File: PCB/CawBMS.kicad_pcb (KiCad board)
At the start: 4 copper layers, 53.5 x 38 mm, 132 parts, among them CN1 SWD, CN2 I2C, CN3 SPI, CN4 USART, CN5 SWD, CN6 WAFER-SH1.0-6PWB, Q1 CSD13381F4, Q10 TP0610K-T1-GE3, Q2 CSD13381F4, Q3 CSD13381F4, Q4 CSD13381F4, Q5 CSD13381F4, Q6 BSC0702LS, Q7 BSC0702LS, Q8 BSC0702LS, Q9 BSC0702LS, SW1 B3U-1000P, SW2 B3U-1000P, SW3 B3U-1000P, U1 STM32F103CBTx, U2 TCAN1044DRBRQ1, U3 TPS61240DRVR, U4 BQ7692003PW, U5 CAN, X1 Crystal_16MHz_15pF_3P

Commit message: Signed-off-by: jasperThinkpad <2567434944@qq.com>
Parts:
- removed R40: 1M, Resistor_SMD:R_0402_1005Metric_Pad0.72x0.64mm_HandSolder
- removed REF**: OSHW-Logo2_9.8x8mm_SilkScreen, Symbol:OSHW-Logo2_9.8x8mm_SilkScreen
- removed U5: CAN, Rick_Connector:CONN-SMD_2P-P1.00_XUNPU_WAFER-SH1.0-2PWB
- added CN7: WAFER-SH1.0-6PWB, Rick_Connector:CONN-SMD_6P-P1.00_XUNPU_WAFER-SH1.0-6PWB, B.Cu at (88.0, 73.0)
- added R11: 0, Resistor_SMD:R_0402_1005Metric_Pad0.72x0.64mm_HandSolder, F.Cu at (101.0, 45.0)
- C10: value 0.22uF -> 4.7uF
- C11, C9: value 0.22uF -> 0.1uF; footprint Capacitor_SMD:C_0402_1005Metric_Pad0.74x0.62mm_HandSolder -> Capacitor_SMD:C_0603_1608Metric_Pad1.08x0.95mm_HandSolder
- C12: value 0.22uF -> 2.2uF
- C15: value 4.7uF -> 470pF
- C16: value 2.2uF -> 1uF
- C17: value 1uF -> 0.22uF
- C18: value 1uF -> 4.7uF
- C19: value 10uF -> 1uF; footprint Capacitor_SMD:C_0603_1608Metric_Pad1.08x0.95mm_HandSolder -> Capacitor_SMD:C_0402_1005Metric_Pad0.74x0.62mm_HandSolder
- C20: value 4.7uF -> 10uF; footprint Capacitor_SMD:C_0402_1005Metric_Pad0.74x0.62mm_HandSolder -> Capacitor_SMD:C_0603_1608Metric_Pad1.08x0.95mm_HandSolder
- C21, C22: value 0.1uF -> 0.22uF
- C24: value 470pF -> 0.1uF
- C25: footprint Capacitor_SMD:C_0603_1608Metric_Pad1.08x0.95mm_HandSolder -> Capacitor_SMD:C_0402_1005Metric_Pad0.74x0.62mm_HandSolder
- C26: value 0.1uF -> 0.22uF; footprint Capacitor_SMD:C_0603_1608Metric_Pad1.08x0.95mm_HandSolder -> Capacitor_SMD:C_0402_1005Metric_Pad0.74x0.62mm_HandSolder
- CN1: value SWD -> CAN; footprint Rick_Connector:CONN-SMD_4P-P1.00_WAFER-SH1.0-4PWB -> Rick_Connector:CONN-SMD_2P-P1.00_XUNPU_WAFER-SH1.0-2PWB
- CN2: value I2C -> SWD
- CN3: value SPI -> I2C; footprint Rick_Connector:CONN-SMD_6P-P1.00_XUNPU_WAFER-SH1.0-6PWB -> Rick_Connector:CONN-SMD_4P-P1.00_WAFER-SH1.0-4PWB
- CN4: value USART -> SPI; footprint Rick_Connector:CONN-SMD_4P-P1.00_WAFER-SH1.0-4PWB -> Rick_Connector:CONN-SMD_6P-P1.00_XUNPU_WAFER-SH1.0-6PWB
- CN5: value SWD -> USART
- CN6: value WAFER-SH1.0-6PWB -> POWER; footprint Rick_Connector:CONN-SMD_6P-P1.00_XUNPU_WAFER-SH1.0-6PWB -> Rick_Connector:CONN-SMD_4P-P1.00_WAFER-SH1.0-4PWB
- D10: value D_200V -> D_Zener_5.6V; footprint Diode_SMD:D_SMA_Handsoldering -> Diode_SMD:D_SOD-523
- D11: value D_100V -> D_Zener_16V; footprint Diode_SMD:D_SOD-323_HandSoldering -> Diode_SMD:D_SOD-523
- D12: value D_Zener_16V -> D_Zener_5.6V
- D4: value D_Zener_5.6V -> TVS_24V; footprint Diode_SMD:D_SOD-523 -> Diode_SMD:D_SMA_Handsoldering
- D5: value D_Zener_5.6V -> D_200V; footprint Diode_SMD:D_SOD-523 -> Diode_SMD:D_SMA_Handsoldering
- D9: value TVS_24V -> D_100V; footprint Diode_SMD:D_SMA_Handsoldering -> Diode_SMD:D_SOD-323_HandSoldering
- H6: value B- -> P+
- H7: value P+ -> B-
- Q10: value TP0610K-T1-GE3 -> BSC0702LS; footprint Package_TO_SOT_SMD:SOT-23 -> Rick_MOSFET:BSC0702LS_PG-TDSON-8_L5.0-W6.0-P1.27-BL-EP
- Q4: value CSD13381F4 -> TP0610K-T1-GE3; footprint Rick_MOSFET:CSD13381F4_PICOSTAR-3_L1.0-W0.6-P0.40-S0.65-BL-1 -> Package_TO_SOT_SMD:SOT-23
- Q6: value BSC0702LS -> CSD13381F4; footprint Rick_MOSFET:BSC0702LS_PG-TDSON-8_L5.0-W6.0-P1.27-BL-EP -> Rick_MOSFET:CSD13381F4_PICOSTAR-3_L1.0-W0.6-P0.40-S0.65-BL-1
- R1: value 10k -> 120
- R12, R15: value 28.7 -> 100
- R14: value 28.7 -> 10k
- R17: value 100 -> 499k
- R19, R27, R31: value 100 -> 10k
- R20: value 10k -> NTC 10k
- R22, R26: value 10k -> 28.7
- R28: value NTC 10k -> 1M
- R29: value 10k -> 100
- R3: value 0 -> 10k
- R30: value 100 -> 28.7
- R32: value 0.0015 -> 1M; footprint Resistor_SMD:R_2512_6332Metric_Pad1.40x3.35mm_HandSolder -> Resistor_SMD:R_0402_1005Metric_Pad0.72x0.64mm_HandSolder
- R33, R34: value 0.0015 -> 100; footprint Resistor_SMD:R_2512_6332Metric_Pad1.40x3.35mm_HandSolder -> Resistor_SMD:R_0402_1005Metric_Pad0.72x0.64mm_HandSolder
- R35: value 100 -> 1M
- R36, R39: value 1M -> 0.0015; footprint Resistor_SMD:R_0402_1005Metric_Pad0.72x0.64mm_HandSolder -> Resistor_SMD:R_2512_6332Metric_Pad1.40x3.35mm_HandSolder
- R37: value 0 -> 100
- R38: value 499k -> 0.0015; footprint Resistor_SMD:R_0402_1005Metric_Pad0.72x0.64mm_HandSolder -> Resistor_SMD:R_2512_6332Metric_Pad1.40x3.35mm_HandSolder
- R6: value 120 -> 10k
- R7: value 510 -> 0
- R8: value 10k -> 510
- U1: value STM32F103CBTx -> SIT1051AT/3; footprint Package_QFP:LQFP-48_7x7mm_P0.5mm -> Rick_CAN:ISO1044BDR_SOP-8
- U2: value TCAN1044DRBRQ1 -> STM32F103C_8-B_Tx; footprint Rick_CAN:TCAN1044DRBRQ1_DFN-8_L3.0-W3.0-P0.65-TL-EP2.4 -> Package_QFP:LQFP-48_7x7mm_P0.5mm
- moved C1 63.7 mm to (107.6, 47.0)
- moved C10 63.7 mm to (92.4, 46.8)
- moved C11 63.7 mm to (92.4, 49.8)
- moved C15 63.7 mm to (105.0, 56.7)
- moved C24 63.7 mm to (102.1, 49.4)
- moved C26 63.7 mm to (105.4, 66.5)
- moved C4 63.7 mm to (107.6, 45.8)
- moved C5 63.7 mm to (120.4, 49.0)
- moved C6 63.7 mm to (105.0, 54.2)
- moved C8 63.7 mm to (105.0, 51.7)
- moved CN5 63.7 mm to (125.8, 48.5)
- moved CN6 63.7 mm to (78.8, 49.8)
- moved L4 63.7 mm to (99.8, 66.5)
- moved L5 63.7 mm to (111.5, 66.5)
- moved Q3 63.7 mm to (86.1, 49.8)
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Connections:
- C1 pad 1: +3.3V -> +5V
- C10 pad 1: /BQ76920/VC4 -> +5V
- C10 pad 2: /BQ76920/VC3 -> GND
- C11 pad 1: /BQ76920/VC3 -> Net-(C11-Pad1)
- C11 pad 2: /BQ76920/VC2 -> PACK-
- C12 pad 1: /BQ76920/VC2 -> +3.3V
- C12 pad 2: /BQ76920/VC1 -> GND
- C13 pad 1: /BQ76920/VC1 -> /BQ76920/VC5
- C13 pad 2: /BQ76920/VC0 -> /BQ76920/VC4
- C14 pad 1: /BQ76920/VC0 -> /BQ76920/VC4
- C14 pad 2: GND -> /BQ76920/VC3
- C15 pad 1: +3.3V -> /ALERT
- C16 pad 1: +3.3V -> GND
- C16 pad 2: GND -> Net-(U4-CAP1)
- C17 pad 1: /BQ76920/BAT -> /BQ76920/VC3
- C17 pad 2: GND -> /BQ76920/VC2
- C18 pad 1: GND -> +3.3V
- C18 pad 2: Net-(U4-CAP1) -> GND
- C19 pad 1: Net-(U4-BAT) -> /BQ76920/BAT
- C20 pad 1: +5V -> Net-(U4-BAT)
- C21 pad 1: GND -> /BQ76920/VC2
- C21 pad 2: /BQ76920/SRP -> /BQ76920/VC1
- C22 pad 1: /BQ76920/SRP -> /BQ76920/VC1
- C22 pad 2: /BQ76920/SRN -> /BQ76920/VC0
- C23 pad 1: /BQ76920/SRN -> GND
- C23 pad 2: GND -> /BQ76920/SRP
- C24 pad 1: /ALERT -> /BQ76920/SRP
- C24 pad 2: GND -> /BQ76920/SRN
- C25 pad 1: Net-(C25-Pad1) -> /BQ76920/SRN
- C25 pad 2: Net-(C25-Pad2) -> GND
- C26 pad 1: Net-(C25-Pad2) -> /BQ76920/VC0
- C26 pad 2: PACK- -> GND
- C27 pad 1: PACK+ -> Net-(C27-Pad1)
- C3 pad 1: +3.3V -> /RESET
- C5 pad 1: +5V -> +3.3V
- C6 pad 1: +3.3VA -> +3.3V
- C8 pad 1: /RESET -> +3.3VA
- C9 pad 1: /BQ76920/VC5 -> PACK+
- C9 pad 2: /BQ76920/VC4 -> Net-(C11-Pad1)
- CN1 pad 1: GND -> /CAN_N
- CN1 pad 2: GND -> /CAN_P
- CN1 pad 3: +3.3V -> unconnected-(CN1-Pad3)
- CN1 pad 4: +5V -> unconnected-(CN1-Pad4)
- CN2 pad 1: /I2C2_SDA -> /SWDIO
- CN2 pad 2: /I2C2_SCL -> /SWCLK
- CN3 pad 1: /SPI1_NSS -> /I2C2_SDA
- CN3 pad 2: /SPI1_SCK -> /I2C2_SCL
- CN3 pad 3: /SPI1_MISO -> GND
- CN3 pad 4: /SPI1_MOSI -> +3.3V
- CN3 pad 5: GND -> unconnected-(CN3-Pad5)
- CN3 pad 6: +3.3V -> unconnected-(CN3-Pad6)
- CN4 pad 1: /USART1_TX -> /SPI1_NSS
- CN4 pad 2: /USART1_RX -> /SPI1_SCK
- CN4 pad 3: GND -> /SPI1_MISO
- CN4 pad 4: +3.3V -> /SPI1_MOSI
- CN4 pad 5: unconnected-(CN4-Pad5) -> GND
- CN4 pad 6: unconnected-(CN4-Pad6) -> +3.3V
- CN5 pad 1: /SWDIO -> /USART1_TX
- CN5 pad 2: /SWCLK -> /USART1_RX
- CN6 pad 1: /BQ76920/BAT -> GND
- CN6 pad 2: Net-(D4-A) -> GND
- CN6 pad 3: Net-(D5-A) -> +3.3V
- CN6 pad 4: Net-(D6-A) -> +5V
- CN6 pad 5: Net-(D7-A) -> unconnected-(CN6-Pad5)
- CN6 pad 6: Net-(D8-A) -> unconnected-(CN6-Pad6)
- D10 pad 1: PACK+ -> Net-(D10-K)
- D10 pad 2: PACK- -> Net-(D10-A)
- D11 pad 2: Net-(D11-A) -> PACK-
- D12 pad 1: Net-(D11-K) -> Net-(D12-K)
- D12 pad 2: PACK- -> Net-(D12-A)
- D4 pad 1: Net-(D4-K) -> -BATT
- D4 pad 2: Net-(D4-A) -> PACK+
- D5 pad 1: Net-(D5-K) -> PACK+
- D5 pad 2: Net-(D5-A) -> PACK-
- D9 pad 1: -BATT -> Net-(D11-K)
- D9 pad 2: PACK+ -> Net-(D9-A)
- H6 pad 1: -BATT -> PACK+
- H7 pad 1: PACK+ -> -BATT
- L3 pad 2: Net-(Q7-G) -> Net-(Q9-G)
- L4 pad 2: Net-(Q6-G) -> Net-(Q7-G)
- L6 pad 2: Net-(Q9-G) -> Net-(Q10-G)
- Q1 pad 1: Net-(D4-K) -> Net-(D6-K)
- Q1 pad 2: Net-(D4-A) -> Net-(D6-A)
- Q10 pad 1: GND -> PACK-
- Q10 pad 2: /BQ76920/CHG -> PACK-
- Q10 pad 3: Net-(D11-A) -> PACK-
- Q2 pad 1: Net-(D5-K) -> Net-(D7-K)
- Q2 pad 2: Net-(D5-A) -> Net-(D7-A)
- Q3 pad 1: Net-(D6-K) -> Net-(D8-K)
- Q3 pad 2: Net-(D6-A) -> Net-(D8-A)
- Q4 pad 1: Net-(D7-K) -> GND
- Q4 pad 2: Net-(D7-A) -> /BQ76920/CHG
- Q4 pad 3: Net-(Q4-D) -> Net-(D9-A)
- Q5 pad 1: Net-(D8-K) -> Net-(D10-K)
- Q5 pad 2: Net-(D8-A) -> Net-(D10-A)
- Q6 pad 1: Net-(C25-Pad1) -> Net-(D12-K)
- Q6 pad 2: Net-(C25-Pad1) -> Net-(D12-A)
- Q6 pad 3: Net-(C25-Pad1) -> Net-(Q6-D)
- Q7 pad 1: Net-(C25-Pad1) -> Net-(C27-Pad1)
- Q7 pad 2: Net-(C25-Pad1) -> Net-(C27-Pad1)
- Q7 pad 3: Net-(C25-Pad1) -> Net-(C27-Pad1)
- Q7 pad 5: Net-(Q6-D-Pad5) -> Net-(Q10-D-Pad5)
- Q7 pad 6: Net-(Q6-D-Pad5) -> Net-(Q10-D-Pad5)
- Q7 pad 7: Net-(Q6-D-Pad5) -> Net-(Q10-D-Pad5)
- Q7 pad 8: Net-(Q6-D-Pad5) -> Net-(Q10-D-Pad5)
- Q8 pad 5: Net-(Q6-D-Pad5) -> Net-(Q10-D-Pad5)
- Q8 pad 6: Net-(Q6-D-Pad5) -> Net-(Q10-D-Pad5)
- Q8 pad 7: Net-(Q6-D-Pad5) -> Net-(Q10-D-Pad5)
- Q8 pad 8: Net-(Q6-D-Pad5) -> Net-(Q10-D-Pad5)
- Q9 pad 1: PACK- -> Net-(C27-Pad1)
- Q9 pad 2: PACK- -> Net-(C27-Pad1)
- Q9 pad 3: PACK- -> Net-(C27-Pad1)
- Q9 pad 5: Net-(Q6-D-Pad5) -> Net-(Q10-D-Pad5)
- Q9 pad 6: Net-(Q6-D-Pad5) -> Net-(Q10-D-Pad5)
- Q9 pad 7: Net-(Q6-D-Pad5) -> Net-(Q10-D-Pad5)
- Q9 pad 8: Net-(Q6-D-Pad5) -> Net-(Q10-D-Pad5)
- R1 pad 1: GND -> /CAN_N
- R1 pad 2: Net-(U1-PB2) -> /CAN_P
- R12 pad 2: Net-(Q1-D) -> /BQ76920/VC5
- R13 pad 1: Net-(D4-A) -> /BQ76920/BAT
- R13 pad 2: Net-(Q2-D) -> Net-(Q1-D)
- R14 pad 1: Net-(D5-A) -> Net-(D6-K)
- R14 pad 2: Net-(Q3-D) -> /BQ76920/VC4
- R15 pad 2: Net-(Q4-D) -> /BQ76920/VC4
- R16 pad 1: Net-(D7-A) -> Net-(D6-A)
- R16 pad 2: Net-(Q5-D) -> Net-(Q2-D)
- R17 pad 1: /BQ76920/BAT -> GND
- R17 pad 2: /BQ76920/VC5 -> /ALERT
- R18 pad 1: Net-(D4-K) -> Net-(D7-K)
- R18 pad 2: /BQ76920/VC4 -> /BQ76920/VC3
- R19 pad 1: Net-(D4-A) -> Net-(R19-Pad1)
- R19 pad 2: /BQ76920/VC4 -> Net-(U4-TS1)
- R2 pad 2: Net-(U1-BOOT0) -> Net-(U2-BOOT0)
- R20 pad 1: Net-(D5-K) -> GND
- R20 pad 2: /BQ76920/VC3 -> Net-(U4-TS1)
- R21 pad 1: Net-(D5-A) -> Net-(D7-A)
- R22 pad 1: Net-(D6-K) -> Net-(D7-A)
- R22 pad 2: /BQ76920/VC2 -> Net-(Q3-D)
- R23 pad 1: Net-(D6-A) -> /BQ76920/BAT
- R23 pad 2: /BQ76920/VC2 -> Net-(U4-BAT)
- R24 pad 1: Net-(D7-K) -> Net-(D8-K)
- R24 pad 2: /BQ76920/VC1 -> /BQ76920/VC2
- R25 pad 1: Net-(D7-A) -> Net-(D8-A)
- R25 pad 2: /BQ76920/VC1 -> /BQ76920/VC2
- R26 pad 1: Net-(D8-K) -> Net-(D8-A)
- R26 pad 2: /BQ76920/VC0 -> Net-(Q5-D)
- R27 pad 1: Net-(D8-A) -> Net-(D10-K)
- R27 pad 2: /BQ76920/VC0 -> /BQ76920/VC1
- R28 pad 1: GND -> Net-(D11-K)
- R28 pad 2: Net-(U4-TS1) -> Net-(D9-A)
- R29 pad 1: Net-(R29-Pad1) -> Net-(D10-A)
- R29 pad 2: Net-(U4-TS1) -> /BQ76920/VC1
- R3 pad 1: Net-(U1-VSSA) -> +3.3V
- R3 pad 2: GND -> /I2C1_SCL
- R30 pad 1: /BQ76920/BAT -> Net-(D10-A)
- R30 pad 2: Net-(U4-BAT) -> Net-(Q6-D)
- R31 pad 1: -BATT -> Net-(D12-K)
- R31 pad 2: /BQ76920/SRP -> /BQ76920/VC0
- R32 pad 1: -BATT -> PACK-
- R32 pad 2: Net-(C25-Pad1) -> Net-(D11-K)
- R33 pad 2: Net-(C25-Pad1) -> /BQ76920/SRP
- R34 pad 1: -BATT -> Net-(C27-Pad1)
- R34 pad 2: Net-(C25-Pad1) -> /BQ76920/SRN
- R35 pad 1: Net-(C25-Pad1) -> Net-(C27-Pad1)
- R35 pad 2: /BQ76920/SRN -> /BQ76920/DSG
- R36 pad 1: Net-(C25-Pad1) -> -BATT
- R36 pad 2: /BQ76920/DSG -> Net-(C27-Pad1)
- R37 pad 1: -BATT -> Net-(D12-A)
- R37 pad 2: GND -> /BQ76920/VC0
- R38 pad 1: GND -> -BATT
- R38 pad 2: /ALERT -> Net-(C27-Pad1)
- R39 pad 1: Net-(D11-K) -> -BATT
- R39 pad 2: Net-(D11-A) -> Net-(C27-Pad1)
- R4 pad 2: /I2C1_SCL -> /I2C1_SDA
- R5 pad 1: +3.3V -> GND
- R5 pad 2: /I2C1_SDA -> Net-(U2-PB2)
- R6 pad 1: /CAN_N -> +3.3V
- R6 pad 2: /CAN_P -> /RESET
- R7 pad 1: Net-(D1-K) -> Net-(U2-VSSA)
- R7 pad 2: /LED_A -> GND
- R8 pad 1: +3.3V -> Net-(D1-K)
- R8 pad 2: /RESET -> /LED_A
- SW3 pad 2: Net-(R29-Pad1) -> Net-(R19-Pad1)
- U1 pad 1: +3.3V -> /CAN_TX
- U1 pad 2: /ALERT -> GND
- U1 pad 3: /LED_A -> +5V
- U1 pad 4: /LED_B -> /CAN_RX
- U1 pad 5: /HSE_IN -> +3.3V
- U1 pad 6: /HSE_OUT -> /CAN_N
- U1 pad 7: /RESET -> /CAN_P
- U1 pad 8: Net-(U1-VSSA) -> /CAN_S
- U2 pad 1: /CAN_TX -> +3.3V
- U2 pad 2: GND -> /ALERT
- U2 pad 3: +5V -> /LED_A
- U2 pad 4: /CAN_RX -> /LED_B
- U2 pad 5: +3.3V -> /HSE_IN
- U2 pad 6: /CAN_N -> /HSE_OUT
- U2 pad 7: /CAN_P -> /RESET
- U2 pad 8: /CAN_STB -> Net-(U2-VSSA)
- U2 pad 9: GND -> +3.3VA
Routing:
- net +5V: track 51.5 -> 0.00 mm, vias 3 -> 0
- net GND: track 48.4 -> 0.00 mm, vias 45 -> 0
- net /BQ76920/BAT: track 43.9 -> 0.00 mm, vias 2 -> 0
- net +3.3V: track 42.2 -> 0.00 mm, vias 22 -> 0
- net /BQ76920/VC1: track 37.2 -> 0.00 mm, vias 2 -> 0
- net /KEY_A: track 34.3 -> 0.00 mm, vias 2 -> 0
- net /RESET: track 28.7 -> 0.00 mm
- net Net-(R29-Pad1): track 26.1 -> 0.00 mm
- net /ALERT: track 25.9 -> 0.00 mm, vias 2 -> 0
- net /I2C1_SDA: track 20.0 -> 0.00 mm, vias 2 -> 0
- net /BQ76920/VC4: track 19.2 -> 0.00 mm
- net /I2C1_SCL: track 18.5 -> 0.00 mm, vias 2 -> 0
- net /BQ76920/VC5: track 18.0 -> 0.00 mm
- net Net-(D8-A): track 17.8 -> 0.00 mm
- net /I2C2_SCL: track 16.9 -> 0.00 mm, vias 2 -> 0
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- removed copper zone on In2.Cu, net +3.3V
- removed copper zone on B.Cu, net -BATT
- removed copper zone on F.Cu, net -BATT
- removed copper zone on In1.Cu, net -BATT
- removed copper zone on In2.Cu, net -BATT
- removed copper zone on In1.Cu, net GND
- removed copper zone on B.Cu, net Net-(C25-Pad1)
- removed copper zone on F.Cu, net Net-(C25-Pad1)
- removed copper zone on In1.Cu, net Net-(C25-Pad1)
- removed copper zone on In2.Cu, net Net-(C25-Pad1)
- removed copper zone on F.Cu, net Net-(Q6-D-Pad5)
- removed copper zone on In1.Cu, net Net-(Q6-D-Pad5)
- removed copper zone on B.Cu, net PACK+
- removed copper zone on F.Cu, net PACK+
- removed copper zone on In1.Cu, net PACK+
- removed copper zone on In2.Cu, net PACK+
- removed copper zone on B.Cu, net PACK-
- removed copper zone on F.Cu, net PACK-
- removed copper zone on In1.Cu, net PACK-
- removed copper zone on In2.Cu, net PACK-

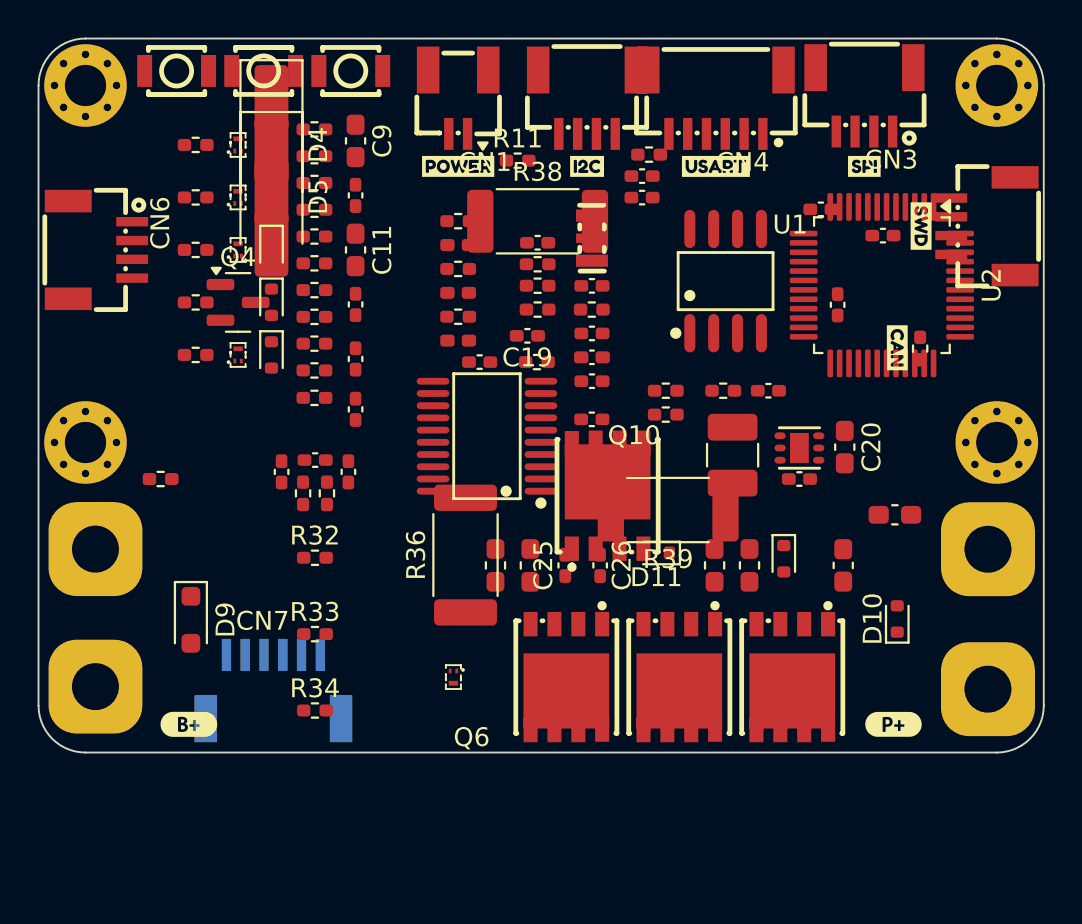
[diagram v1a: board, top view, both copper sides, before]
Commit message: 3.5 布局完成
Signed-off-by: jasper <2567434944@qq.com>
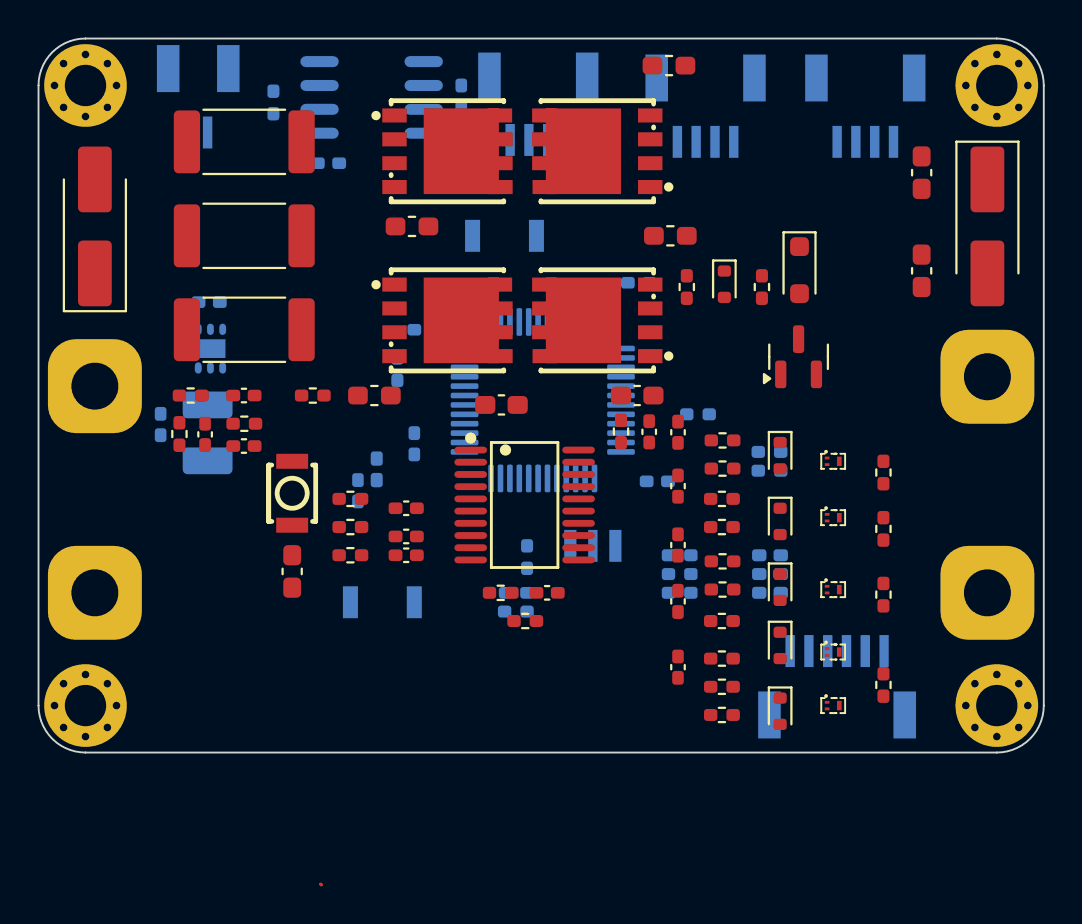
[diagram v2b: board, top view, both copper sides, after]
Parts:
- removed CN6: POWER, Rick_Connector:CONN-SMD_4P-P1.00_WAFER-SH1.0-4PWB
- removed CN7: WAFER-SH1.0-6PWB, Rick_Connector:CONN-SMD_6P-P1.00_XUNPU_WAFER-SH1.0-6PWB
- removed G***: LOGO, Rick_Logo:guaik_logo_black_8x8
- removed kibuzzard-6577EBC9: G***, kibuzzard-6577EBC9
- removed kibuzzard-6577F12B: G***, kibuzzard-6577F12B
- removed kibuzzard-6577F182: G***, kibuzzard-6577F182
- removed kibuzzard-6577F8B5: G***, kibuzzard-6577F8B5
- removed kibuzzard-6582907D: G***, kibuzzard-6582907D
- removed kibuzzard-65829086: G***, kibuzzard-65829086
- removed kibuzzard-65902364: G***, kibuzzard-65902364
- added kibuzzard-67C7CF73: G***, kibuzzard-67C7CF73, B.Cu at (97.0, 73.5)
- C1, C2, C3, C6, C7, C8, CN2, D1, D2, D3, R1, R10, R2, R3, R4, R5, R6, R7, R8, R9, U1, U2, U3, X1, kibuzzard-6577EBAB, kibuzzard-6577EC0F, kibuzzard-6577EC47, kibuzzard-658FE662, kibuzzard-658FE679: moved to B.Cu
- C10: value 4.7uF -> 0.1uF; moved to B.Cu
- C12: value 2.2uF -> 0.1uF; footprint Capacitor_SMD:C_0402_1005Metric_Pad0.74x0.62mm_HandSolder -> Capacitor_SMD:C_0603_1608Metric_Pad1.08x0.95mm_HandSolder
- C13: value 0.22uF -> 470pF
- C14, C17: value 0.22uF -> 1uF
- C15: value 470pF -> 0.22uF
- C16: value 1uF -> 4.7uF
- C18: value 4.7uF -> 10uF; footprint Capacitor_SMD:C_0402_1005Metric_Pad0.74x0.62mm_HandSolder -> Capacitor_SMD:C_0603_1608Metric_Pad1.08x0.95mm_HandSolder
- C19: value 1uF -> 0.22uF
- C20: value 10uF -> 0.22uF; footprint Capacitor_SMD:C_0603_1608Metric_Pad1.08x0.95mm_HandSolder -> Capacitor_SMD:C_0402_1005Metric_Pad0.74x0.62mm_HandSolder
- C22: value 0.22uF -> 0.1uF
- C25: value 0.1uF -> 0.22uF
- C4: value 0.1uF -> 4.7uF; moved to B.Cu
- C5: value 0.1uF -> 2.2uF; moved to B.Cu
- C9: footprint Capacitor_SMD:C_0603_1608Metric_Pad1.08x0.95mm_HandSolder -> Capacitor_SMD:C_0402_1005Metric_Pad0.74x0.62mm_HandSolder; moved to B.Cu
- CN1: value CAN -> USART; footprint Rick_Connector:CONN-SMD_2P-P1.00_XUNPU_WAFER-SH1.0-2PWB -> Rick_Connector:CONN-SMD_4P-P1.00_WAFER-SH1.0-4PWB; moved to B.Cu
- CN3: value I2C -> CAN; footprint Rick_Connector:CONN-SMD_4P-P1.00_WAFER-SH1.0-4PWB -> Rick_Connector:CONN-SMD_2P-P1.00_XUNPU_WAFER-SH1.0-2PWB; moved to B.Cu
- CN4: value SPI -> POWER; footprint Rick_Connector:CONN-SMD_6P-P1.00_XUNPU_WAFER-SH1.0-6PWB -> Rick_Connector:CONN-SMD_4P-P1.00_WAFER-SH1.0-4PWB; moved to B.Cu
- CN5: value USART -> WAFER-SH1.0-6PWB; footprint Rick_Connector:CONN-SMD_4P-P1.00_WAFER-SH1.0-4PWB -> Rick_Connector:CONN-SMD_6P-P1.00_XUNPU_WAFER-SH1.0-6PWB; moved to B.Cu
- D10: value D_Zener_5.6V -> D_Zener_16V
- D11: value D_Zener_16V -> D_Zener_5.6V
- D8: value D_Zener_5.6V -> D_100V; footprint Diode_SMD:D_SOD-523 -> Diode_SMD:D_SOD-323_HandSoldering
- D9: value D_100V -> D_Zener_5.6V; footprint Diode_SMD:D_SOD-323_HandSoldering -> Diode_SMD:D_SOD-523
- H6: value P+ -> B-
- H7: value B- -> P+
- L1: value 39nH -> 1uH; footprint Inductor_SMD:L_0402_1005Metric_Pad0.77x0.64mm_HandSolder -> Inductor_SMD:L_1210_3225Metric_Pad1.42x2.65mm_HandSolder; moved to B.Cu
- L2: value 1uH -> 39nH; footprint Inductor_SMD:L_1210_3225Metric_Pad1.42x2.65mm_HandSolder -> Inductor_SMD:L_0402_1005Metric_Pad0.77x0.64mm_HandSolder; moved to B.Cu
- Q3: value CSD13381F4 -> TP0610K-T1-GE3; footprint Rick_MOSFET:CSD13381F4_PICOSTAR-3_L1.0-W0.6-P0.40-S0.65-BL-1 -> Package_TO_SOT_SMD:SOT-23
- Q4: value TP0610K-T1-GE3 -> CSD13381F4; footprint Package_TO_SOT_SMD:SOT-23 -> Rick_MOSFET:CSD13381F4_PICOSTAR-3_L1.0-W0.6-P0.40-S0.65-BL-1
- Q6: value CSD13381F4 -> BSC0702LS; footprint Rick_MOSFET:CSD13381F4_PICOSTAR-3_L1.0-W0.6-P0.40-S0.65-BL-1 -> Rick_MOSFET:BSC0702LS_PG-TDSON-8_L5.0-W6.0-P1.27-BL-EP
- Q8: value BSC0702LS -> CSD13381F4; footprint Rick_MOSFET:BSC0702LS_PG-TDSON-8_L5.0-W6.0-P1.27-BL-EP -> Rick_MOSFET:CSD13381F4_PICOSTAR-3_L1.0-W0.6-P0.40-S0.65-BL-1
- R12: value 100 -> 499k
- R13: value 28.7 -> 10k
- R14: value 10k -> NTC 10k
- R17: value 499k -> 100
- R19, R31: value 10k -> 100
- R20: value NTC 10k -> 28.7
- R21: value 100 -> 10k
- R22, R26, R30: value 28.7 -> 100
- R23: value 100 -> 28.7
- R25, R29: value 100 -> 1M
- R27: value 10k -> 28.7
- R28: value 1M -> 10k
- R34, R37: value 100 -> 0.0015; footprint Resistor_SMD:R_0402_1005Metric_Pad0.72x0.64mm_HandSolder -> Resistor_SMD:R_2512_6332Metric_Pad1.40x3.35mm_HandSolder
- R35: value 1M -> 28.7
- R38: value 0.0015 -> 10k; footprint Resistor_SMD:R_2512_6332Metric_Pad1.40x3.35mm_HandSolder -> Resistor_SMD:R_0402_1005Metric_Pad0.72x0.64mm_HandSolder
- R39: value 0.0015 -> 100; footprint Resistor_SMD:R_2512_6332Metric_Pad1.40x3.35mm_HandSolder -> Resistor_SMD:R_0402_1005Metric_Pad0.72x0.64mm_HandSolder
- SW1, SW2: value B3U-1000P -> pro:7de6de4c8dc5470396d8d3e1a8ec5922; moved to B.Cu
- SW3: value B3U-1000P -> pro:7de6de4c8dc5470396d8d3e1a8ec5922
- moved Q1 43.5 mm to (117.8, 74.0), turned to -90 degrees
- moved Q2 39.9 mm to (117.8, 71.2), turned to -90 degrees
- moved C5 39.7 mm to (82.0, 59.0), turned to 90 degrees
- moved R20 39.5 mm to (120.5, 72.9), turned to 90 degrees
- moved kibuzzard-6577EC47 38.4 mm to (84.0, 45.6), turned to 180 degrees
- moved D5 38.1 mm to (126.0, 48.5)
- moved D6 36.6 mm to (115.0, 74.3)
- moved R19 35.7 mm to (111.9, 74.5), turned to 180 degrees
- moved R18 35.6 mm to (111.9, 73.0), turned to 180 degrees
- moved CN3 35.5 mm to (84.0, 41.8), turned to 0 degrees
- moved Q4 35.2 mm to (117.8, 67.8), turned to -90 degrees
- moved R23 34.3 mm to (120.5, 68.1), turned to 90 degrees
- moved Q5 32.8 mm to (117.8, 64.0), turned to -90 degrees
- moved D7 32.7 mm to (115.0, 70.8)
- moved U3 31.8 mm to (84.7, 55.0), turned to -90 degrees
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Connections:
- C10 pad 1: +5V -> +3.3VA
- C11 pad 1: Net-(C11-Pad1) -> PACK+
- C11 pad 2: PACK- -> Net-(C11-Pad2)
- C12 pad 1: +3.3V -> Net-(C11-Pad2)
- C12 pad 2: GND -> PACK-
- C13 pad 1: /BQ76920/VC5 -> /ALERT
- C13 pad 2: /BQ76920/VC4 -> GND
- C14 pad 1: /BQ76920/VC4 -> GND
- C14 pad 2: /BQ76920/VC3 -> Net-(U4-CAP1)
- C15 pad 1: /ALERT -> /BQ76920/VC5
- C15 pad 2: GND -> /BQ76920/VC4
- C16 pad 1: GND -> +3.3V
- C16 pad 2: Net-(U4-CAP1) -> GND
- C17 pad 1: /BQ76920/VC3 -> /BQ76920/BAT
- C17 pad 2: /BQ76920/VC2 -> GND
- C18 pad 1: +3.3V -> Net-(U4-BAT)
- C19 pad 1: /BQ76920/BAT -> /BQ76920/VC4
- C19 pad 2: GND -> /BQ76920/VC3
- C20 pad 1: Net-(U4-BAT) -> /BQ76920/VC3
- C20 pad 2: GND -> /BQ76920/VC2
- C22 pad 1: /BQ76920/VC1 -> GND
- C22 pad 2: /BQ76920/VC0 -> /BQ76920/SRP
- C23 pad 1: GND -> /BQ76920/SRP
- C23 pad 2: /BQ76920/SRP -> /BQ76920/SRN
- C24 pad 1: /BQ76920/SRP -> /BQ76920/SRN
- C24 pad 2: /BQ76920/SRN -> GND
- C25 pad 1: /BQ76920/SRN -> /BQ76920/VC1
- C25 pad 2: GND -> /BQ76920/VC0
- C4 pad 1: +3.3V -> +5V
- C8 pad 1: +3.3VA -> +3.3V
- C9 pad 1: PACK+ -> +3.3V
- C9 pad 2: Net-(C11-Pad1) -> GND
- CN1 pad 1: /CAN_N -> /USART1_TX
- CN1 pad 2: /CAN_P -> /USART1_RX
- CN1 pad 3: unconnected-(CN1-Pad3) -> GND
- CN1 pad 4: unconnected-(CN1-Pad4) -> +3.3V
- CN3 pad 1: /I2C2_SDA -> /CAN_N
- CN3 pad 2: /I2C2_SCL -> /CAN_P
- CN3 pad 3: GND -> unconnected-(CN3-Pad3)
- CN3 pad 4: +3.3V -> unconnected-(CN3-Pad4)
- CN4 pad 1: /SPI1_NSS -> GND
- CN4 pad 2: /SPI1_SCK -> GND
- CN4 pad 3: /SPI1_MISO -> +3.3V
- CN4 pad 4: /SPI1_MOSI -> +5V
- CN4 pad 5: GND -> unconnected-(CN4-Pad5)
- CN4 pad 6: +3.3V -> unconnected-(CN4-Pad6)
- CN5 pad 1: /USART1_TX -> /BQ76920/BAT
- CN5 pad 2: /USART1_RX -> Net-(D6-A)
- CN5 pad 3: GND -> Net-(D7-A)
- CN5 pad 4: +3.3V -> Net-(D9-A)
- CN5 pad 5: unconnected-(CN5-Pad5) -> Net-(D11-A)
- CN5 pad 6: unconnected-(CN5-Pad6) -> Net-(D12-A)
- D10 pad 2: Net-(D10-A) -> PACK-
- D11 pad 2: PACK- -> Net-(D11-A)
- D8 pad 1: Net-(D8-K) -> Net-(D10-K)
- D9 pad 1: Net-(D11-K) -> Net-(D9-K)
- H6 pad 1: PACK+ -> -BATT
- H7 pad 1: -BATT -> PACK+
- L1 pad 2: +3.3VA -> Net-(U3-L)
- L2 pad 2: Net-(U3-L) -> +3.3VA
- L4 pad 2: Net-(Q7-G) -> Net-(Q6-G)
- L5 pad 1: Net-(D11-K) -> Net-(D10-K)
- L5 pad 2: Net-(Q8-G) -> Net-(Q7-G)
- L6 pad 1: Net-(D11-K) -> Net-(D10-K)
- Q3 pad 1: Net-(D8-K) -> GND
- Q3 pad 2: Net-(D8-A) -> /BQ76920/CHG
- Q3 pad 3: Net-(Q3-D) -> Net-(D8-A)
- Q4 pad 1: GND -> Net-(D9-K)
- Q4 pad 2: /BQ76920/CHG -> Net-(D9-A)
- Q4 pad 3: Net-(D9-A) -> Net-(Q4-D)
- Q5 pad 1: Net-(D10-K) -> Net-(D11-K)
- Q5 pad 2: Net-(D10-A) -> Net-(D11-A)
- Q6 pad 1: Net-(D12-K) -> Net-(C27-Pad1)
- Q6 pad 2: Net-(D12-A) -> Net-(C27-Pad1)
- Q6 pad 3: Net-(Q6-D) -> Net-(C27-Pad1)
- Q7 pad 1: Net-(C27-Pad1) -> PACK-
- Q7 pad 2: Net-(C27-Pad1) -> PACK-
- Q7 pad 3: Net-(C27-Pad1) -> PACK-
- Q8 pad 1: PACK- -> Net-(D12-K)
- Q8 pad 2: PACK- -> Net-(D12-A)
- Q8 pad 3: PACK- -> Net-(Q8-D)
- R12 pad 1: /BQ76920/BAT -> GND
- R12 pad 2: /BQ76920/VC5 -> /ALERT
- R13 pad 1: /BQ76920/BAT -> Net-(R13-Pad1)
- R13 pad 2: Net-(Q1-D) -> Net-(U4-TS1)
- R14 pad 1: Net-(D6-K) -> GND
- R14 pad 2: /BQ76920/VC4 -> Net-(U4-TS1)
- R15 pad 1: Net-(D6-A) -> /BQ76920/BAT
- R15 pad 2: /BQ76920/VC4 -> /BQ76920/VC5
- R16 pad 1: Net-(D6-A) -> /BQ76920/BAT
- R16 pad 2: Net-(Q2-D) -> Net-(Q1-D)
- R17 pad 1: GND -> /BQ76920/BAT
- R17 pad 2: /ALERT -> Net-(U4-BAT)
- R18 pad 1: Net-(D7-K) -> Net-(D6-K)
- R18 pad 2: /BQ76920/VC3 -> /BQ76920/VC4
- R19 pad 1: Net-(R19-Pad1) -> Net-(D6-A)
- R19 pad 2: Net-(U4-TS1) -> /BQ76920/VC4
- R20 pad 1: GND -> Net-(D6-A)
- R20 pad 2: Net-(U4-TS1) -> Net-(Q2-D)
- R21 pad 1: Net-(D7-A) -> Net-(D7-K)
- R22 pad 2: Net-(Q3-D) -> /BQ76920/VC3
- R23 pad 1: /BQ76920/BAT -> Net-(D7-A)
- R23 pad 2: Net-(U4-BAT) -> Net-(Q4-D)
- R24 pad 1: Net-(D8-K) -> Net-(D9-K)
- R25 pad 1: Net-(D8-A) -> Net-(D10-K)
- R25 pad 2: /BQ76920/VC2 -> Net-(D8-A)
- R26 pad 1: Net-(D8-A) -> Net-(D9-A)
- R26 pad 2: Net-(Q5-D) -> /BQ76920/VC2
- R27 pad 1: Net-(D10-K) -> Net-(D9-A)
- R27 pad 2: /BQ76920/VC1 -> Net-(Q5-D)
- R28 pad 2: Net-(D9-A) -> /BQ76920/VC1
- R29 pad 1: Net-(D10-A) -> PACK-
- R29 pad 2: /BQ76920/VC1 -> Net-(D10-K)
- R30 pad 1: Net-(D10-A) -> -BATT
- R30 pad 2: Net-(Q6-D) -> /BQ76920/SRP
- R31 pad 1: Net-(D12-K) -> Net-(C27-Pad1)
- R31 pad 2: /BQ76920/VC0 -> /BQ76920/SRN
- R32 pad 1: PACK- -> Net-(C27-Pad1)
- R32 pad 2: Net-(D11-K) -> /BQ76920/DSG
- R33 pad 1: -BATT -> Net-(D11-A)
- R33 pad 2: /BQ76920/SRP -> /BQ76920/VC1
- R34 pad 1: Net-(C27-Pad1) -> -BATT
- R34 pad 2: /BQ76920/SRN -> Net-(C27-Pad1)
- R35 pad 1: Net-(C27-Pad1) -> Net-(D11-A)
- R35 pad 2: /BQ76920/DSG -> Net-(Q8-D)
- R37 pad 1: Net-(D12-A) -> -BATT
- R37 pad 2: /BQ76920/VC0 -> Net-(C27-Pad1)
- R38 pad 1: -BATT -> Net-(D12-K)
- R38 pad 2: Net-(C27-Pad1) -> /BQ76920/VC0
- R39 pad 1: -BATT -> Net-(D12-A)
- R39 pad 2: Net-(C27-Pad1) -> /BQ76920/VC0
- SW3 pad 2: Net-(R19-Pad1) -> Net-(R13-Pad1)
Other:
- copper layers 4 -> 2
